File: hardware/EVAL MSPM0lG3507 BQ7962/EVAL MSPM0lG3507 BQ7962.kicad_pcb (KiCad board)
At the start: 2 copper layers, 72.5 x 101.3 mm, 155 parts, among them J1 Conn_01x09_Socket, J10 Screw_Terminal_01x02, J11 Screw_Terminal_01x02, J12 Screw_Terminal_01x02, J13 Screw_Terminal_01x02, J14 Screw_Terminal_01x02, J16 Conn_02x02_Odd_Even, J17 Conn_01x02_Pin, J18 Conn_01x02_Pin, J2 Conn_02x05_Odd_Even, J3 Conn_01x04_Pin, J4 Screw_Terminal_01x02, J5 Conn_01x03_Pin, J7 Screw_Terminal_01x02, J8 Screw_Terminal_01x02, J9 Screw_Terminal_01x02, SW1 SW_Push, SW2 SW_Push, SW3 SW_Push, U1 TPD6E004RSER, U10 MCP2542FDxMF, U11 FCX495, U2 MCU-MSM0G3507SPM, U3 TPD6E004RSER, U4 FCX495, U7 PBQ76952PFBT, U8 FCX495, U9 LMR51603XDBVR

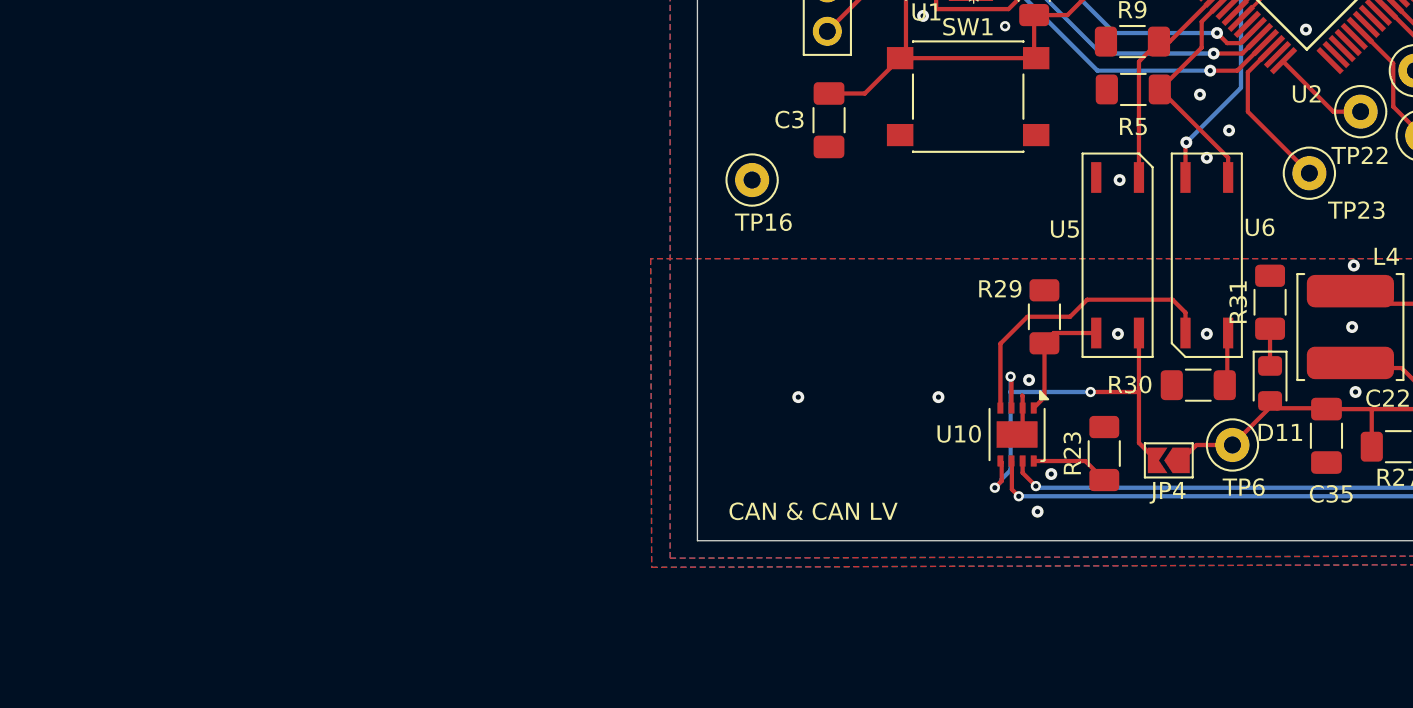
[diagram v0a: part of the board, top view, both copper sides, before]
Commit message: 07/15/25 - PCB Update
- Added the new footprint to the PCB file

Co-Authored-By: Görge Albrecht <617230+goerge@users.noreply.github.com>
Co-Authored-By: MarcusTurley <86125719+MarcusTurley@users.noreply.github.com>
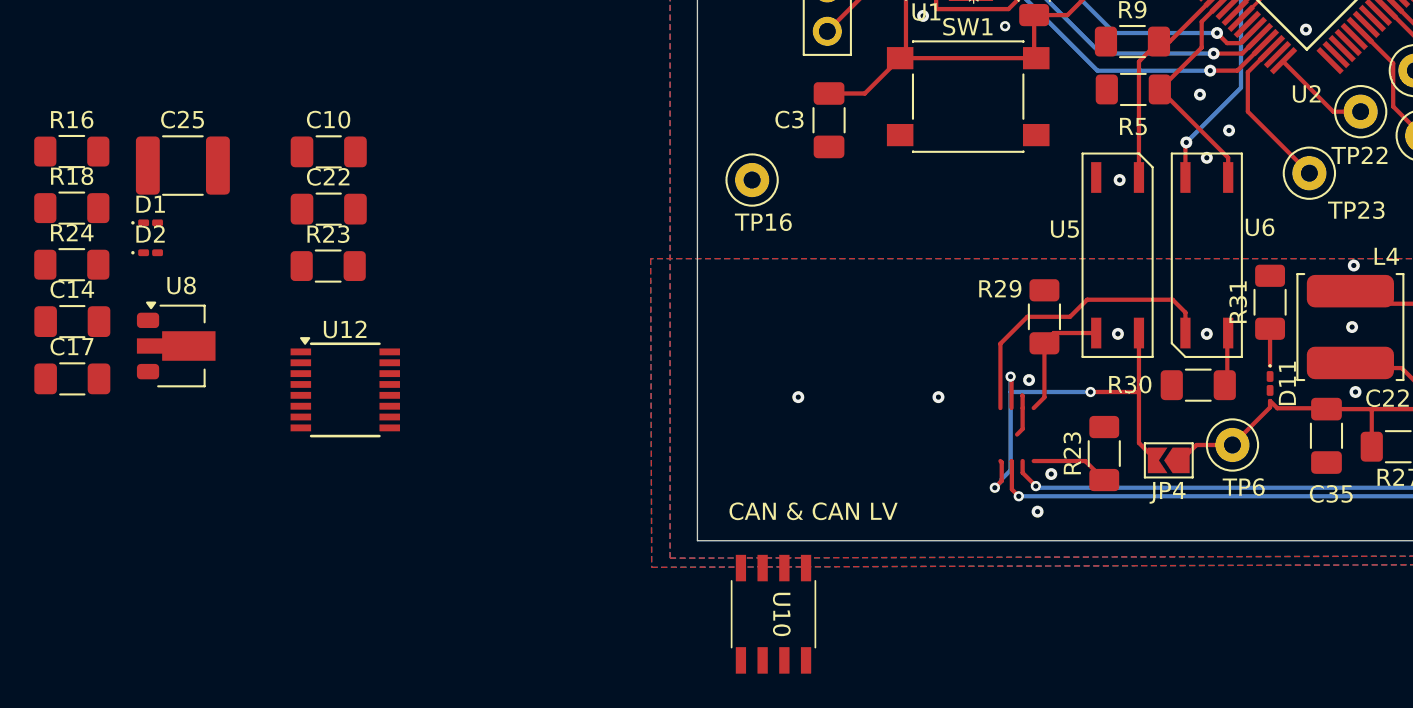
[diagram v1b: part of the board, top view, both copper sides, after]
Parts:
- added C10: 10u, Capacitor_SMD:C_1206_3216Metric_Pad1.33x1.80mm_HandSolder, F.Cu at (80.6, 102.4)
- added C14: 10u, Capacitor_SMD:C_1206_3216Metric_Pad1.33x1.80mm_HandSolder, F.Cu at (65.6, 112.3)
- added C17: 10u, Capacitor_SMD:C_1206_3216Metric_Pad1.33x1.80mm_HandSolder, F.Cu at (65.6, 115.6)
- added C22: 220n, Capacitor_SMD:C_1206_3216Metric_Pad1.33x1.80mm_HandSolder, F.Cu at (80.6, 105.7)
- added C25: 1u, Capacitor_SMD:C_1812_4532Metric, F.Cu at (72.1, 103.2)
- added D1: LED, LED_SMD:LED_0201_0603Metric_Pad0.64x0.40mm_HandSolder, F.Cu at (70.2, 106.5)
- added D2: LED, LED_SMD:LED_0201_0603Metric_Pad0.64x0.40mm_HandSolder, F.Cu at (70.2, 108.3)
- added R16: 5k, Resistor_SMD:R_1206_3216Metric_Pad1.30x1.75mm_HandSolder, F.Cu at (65.6, 102.3)
- added R18: 5k, Resistor_SMD:R_1206_3216Metric_Pad1.30x1.75mm_HandSolder, F.Cu at (65.6, 105.6)
- added R23: 50k, Resistor_SMD:R_1206_3216Metric_Pad1.30x1.75mm_HandSolder, F.Cu at (80.6, 109.0)
- added R24: 50k, Resistor_SMD:R_1206_3216Metric_Pad1.30x1.75mm_HandSolder, F.Cu at (65.6, 109.0)
- added U12: FT230XS, Package_SO:SSOP-16_3.9x4.9mm_P0.635mm, F.Cu at (81.6, 116.3)
- added U8: FCX495, Package_TO_SOT_SMD:SOT-89-3, F.Cu at (72.0, 113.7)
- C35: value 220n -> 10u
- D11: footprint LED_SMD:LED_0805_2012Metric_Pad1.15x1.40mm_HandSolder -> LED_SMD:LED_0201_0603Metric_Pad0.64x0.40mm_HandSolder
- R7: value 47k -> 50k
- U10: footprint Package_DFN_QFN:DFN-8-1EP_3x3mm_P0.65mm_EP1.55x2.4mm -> zzLocalLibraries-Footprints:SOIC-8_4.9x6.0mm_P1.27mm
- moved U10 17.7 mm to (106.6, 129.4)
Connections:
- C26 pad 1: Net-(D5-K) -> Net-(U7-BAT)
- C28 pad 1: Net-(D5-K) -> Net-(C28-Pad1)
- C39 pad 1: Net-(D5-K) -> Net-(U7-BAT)
- C40 pad 1: Net-(D5-K) -> Net-(U7-BAT)
- C41 pad 1: Net-(D5-K) -> Net-(U7-BAT)
- J1 pad 9: PA18 -> unconnected-(J1-Pin_9-Pad9)
- R1 pad 1: Net-(D4-K) -> Net-(D2-K)
- R11 pad 1: Net-(D5-K) -> Net-(U7-BAT)
- R11 pad 2: Net-(R11-Pad2) -> Net-(C25-Pad1)
- R47 pad 2: Net-(D5-K) -> Net-(U7-BAT)
- R49 pad 1: Net-(D5-K) -> Net-(U7-BAT)
- R6 pad 2: Net-(D3-K) -> Net-(D1-K)
- U1 pad 7: PA18 -> /XDS_BLS_INVOKE
- U4 pad 2: Net-(C42-Pad1) -> Net-(C25-Pad1)
- U7 pad 47: Net-(D5-K) -> Net-(U7-BAT)
- U9 pad 4: /GLV CAN TRX/+GLV regulated -> /GLV CAN TRX/+GLV
- U9 pad 5: /GLV CAN TRX/+GLV regulated -> /GLV CAN TRX/+GLV

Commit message: corrected MCP2542FS SOIC footprint pin numbering
marcus almost had it perfect. pads were in wrong order.

Co-Authored-By: George Boone <yongboone1@gmail.com>
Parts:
- turned U10 to 0 degrees
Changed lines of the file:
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@@
 	(footprint "zzLocalLibraries-Footprints:SOIC-8_4.9x6.0mm_P1.27mm"
 		(layer "F.Cu")
-		(at 106.6 129.4 -90)
+		(at 106.6 129.4)
 		(property "Reference" "U10"
-			(at 0 -0.5 270)
+			(at 0 -0.499999 0)
 			(unlocked yes)
 			(layer "F.SilkS")
@@
 		)
 		(property "Value" "MCP2542FDxMF"
-			(at 0 1 270)
+			(at 0 1 0)
 			(unlocked yes)
 			(layer "F.Fab")
@@
 		)
 		(property "Datasheet" "http://ww1.microchip.com/downloads/en/DeviceDoc/MCP2542FD-4FD-MCP2542WFD-4WFD-Data-Sheet20005514B.pdf"
-			(at 0 0 270)
+			(at 0 0 0)
 			(unlocked yes)
 			(layer "F.Fab")
@@
 		)
 		(property "Description" "CAN-FD Transceiver, Wake-Up on CAN activity, 8Mbps, 5V supply, STBY pin, 3x3 DFN-8"
-			(at 0 0 270)
+			(at 0 0 0)
 			(unlocked yes)
 			(layer "F.Fab")
@@
 		)
 		(property "Sim.Device" ""
-			(at 0 0 270)
+			(at 0 0 0)
 			(unlocked yes)
 			(layer "F.Fab")
@@
 		)
 		(property "Sim.Type" ""
-			(at 0 0 270)
+			(at 0 0 0)
 			(unlocked yes)
 			(layer "F.Fab")
@@
 		)
 		(fp_line
+			(start -3.55 -2.345)
+			(end -3.55 2.255)
+			(stroke
+				(width 0.05)
+				(type default)
+			)
+			(layer "F.CrtYd")
+		)
+		(fp_line
+			(start -3.55 2.255)
+			(end -1.95 2.255)
+			(stroke
+				(width 0.05)
+				(type default)
+			)
+			(layer "F.CrtYd")
+		)
+		(fp_line
+			(start -1.95 -2.545)
+			(end -1.95 -2.345)
+			(stroke
+				(width 0.05)
+				(type default)
+			)
+			(layer "F.CrtYd")
+		)
+		(fp_line
+			(start -1.95 -2.345)
+			(end -3.55 -2.345)
+			(stroke
+				(width 0.05)
+				(type default)
+			)
+			(layer "F.CrtYd")
+		)
+		(fp_line
+			(start -1.95 2.255)
+			(end -1.95 2.455)
+			(stroke
+				(width 0.05)
+				(type default)
+			)
+			(layer "F.CrtYd")
+		)
+		(fp_line
 			(start -1.95 2.455)
 			(end 1.95 2.455)
@@
 		)
 		(fp_line
+			(start 1.95 -2.545)
+			(end -1.95 -2.545)
+			(stroke
+				(width 0.05)
+				(type default)
+			)
+			(layer "F.CrtYd")
+		)
+		(fp_line
+			(start 1.95 -2.345)
+			(end 1.95 -2.545)
+			(stroke
+				(width 0.05)
+				(type default)
+			)
+			(layer "F.CrtYd")
+		)
+		(fp_line
 			(start 1.95 2.455)
 			(end 1.95 2.255)
@@
 		)
 		(fp_line
-			(start -3.55 2.255)
-			(end -1.95 2.255)
-			(stroke
-				(width 0.05)
-				(type default)
-			)
-			(layer "F.CrtYd")
-		)
-		(fp_line
-			(start -1.95 2.255)
-			(end -1.95 2.455)
-			(stroke
-				(width 0.05)
-				(type default)
-			)
-			(layer "F.CrtYd")
-		)
-		(fp_line
-			(start 1.95 2.255)
-			(end 3.55 2.255)
-			(stroke
-				(width 0.05)
-				(type default)
-			)
-			(layer "F.CrtYd")
-		)
-		(fp_line
-			(start 3.55 2.255)
-			(end 3.55 -2.345)
-			(stroke
-				(width 0.05)
-				(type default)
-			)
-			(layer "F.CrtYd")
-		)
-		(fp_line
-			(start -3.55 -2.345)
-			(end -3.55 2.255)
-			(stroke
-				(width 0.05)
-				(type default)
-			)
-			(layer "F.CrtYd")
-		)
-		(fp_line
-			(start -1.95 -2.345)
-			(end -3.55 -2.345)
-			(stroke
-				(width 0.05)
-				(type default)
-			)
-			(layer "F.CrtYd")
-		)
-		(fp_line
-			(start 1.95 -2.345)
-			(end 1.95 -2.545)
-			(stroke
-				(width 0.05)
-				(type default)
-			)
-			(layer "F.CrtYd")
-		)
-		(fp_line
 			(start 3.55 -2.345)
 			(end 1.95 -2.345)
@@
 		)
 		(fp_line
-			(start -1.95 -2.545)
-			(end -1.95 -2.345)
-			(stroke
-				(width 0.05)
-				(type default)
-			)
-			(layer "F.CrtYd")
-		)
-		(fp_line
-			(start 1.95 -2.545)
-			(end -1.95 -2.545)
+			(start 3.55 2.25)
+			(end 1.95 2.25)
+			(stroke
+				(width 0.05)
+				(type default)
+			)
+			(layer "F.CrtYd")
+		)
+		(fp_line
+			(start 3.55 2.25)
+			(end 3.55 -2.345)
 			(stroke
 				(width 0.05)
@@
 		)
 		(fp_text user "${REFERENCE}"
-			(at 0 2.5 270)
+			(at 0 2.5 0)
 			(unlocked yes)
 			(layer "F.Fab")
@@
 		)
 		(pad "1" smd rect
-			(at -2.7 -1.955 270)
+			(at -2.7 -1.955)
 			(size 1.55 0.6)
 			(layers "F.Cu" "F.Mask" "F.Paste")
@@
 		)
 		(pad "2" smd rect
-			(at -2.7 -0.685 270)
+			(at -2.7 -0.685)
 			(size 1.55 0.6)
 			(layers "F.Cu" "F.Mask" "F.Paste")
@@
 		)
 		(pad "3" smd rect
-			(at -2.7 0.585 270)
+			(at -2.7 0.585)
 			(size 1.55 0.6)
 			(layers "F.Cu" "F.Mask" "F.Paste")
@@
 		)
 		(pad "4" smd rect
-			(at -2.7 1.855 270)
+			(at -2.7 1.855)
 			(size 1.55 0.6)
 			(layers "F.Cu" "F.Mask" "F.Paste")
@@
 		)
 		(pad "5" smd rect
-			(at 2.7 -1.955 270)
+			(at 2.7 1.86 180)
 			(size 1.55 0.6)
 			(layers "F.Cu" "F.Mask" "F.Paste")
@@
 		)
 		(pad "6" smd rect
-			(at 2.7 0.585 270)
+			(at 2.7 0.58)
 			(size 1.55 0.6)
 			(layers "F.Cu" "F.Mask" "F.Paste")
@@
 		)
 		(pad "7" smd rect
-			(at 2.7 -0.685 270)
+			(at 2.7 -0.69)
 			(size 1.55 0.6)
 			(layers "F.Cu" "F.Mask" "F.Paste")
@@
 		)
 		(pad "8" smd rect
-			(at 2.7 1.855 270)
-			(size 1.55 0.6)
-			(layers "F.Cu" "F.Mask" "F.Paste")
+			(at 2.7 -1.95 180)
+			(size 1.55 0.6)
+			(layers "F.Cu" "F.Mask" "F.Paste")

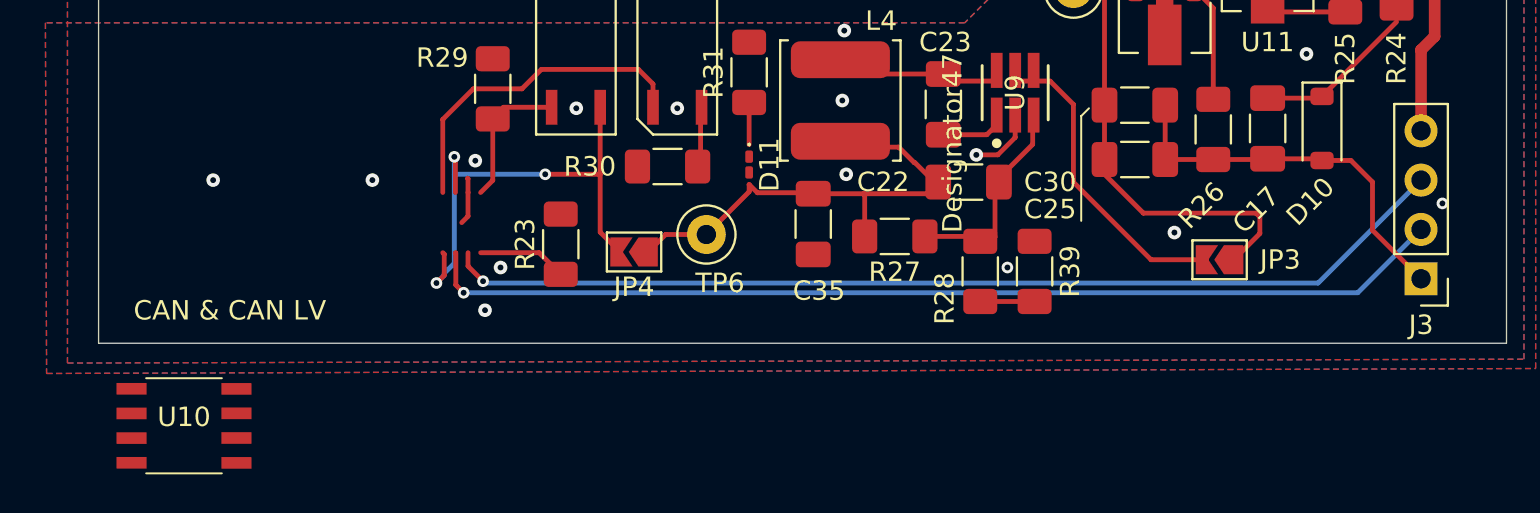
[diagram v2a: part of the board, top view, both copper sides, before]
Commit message: made a hierarchical sheet for the BQ chip
Co-Authored-By: George Boone <yongboone1@gmail.com>
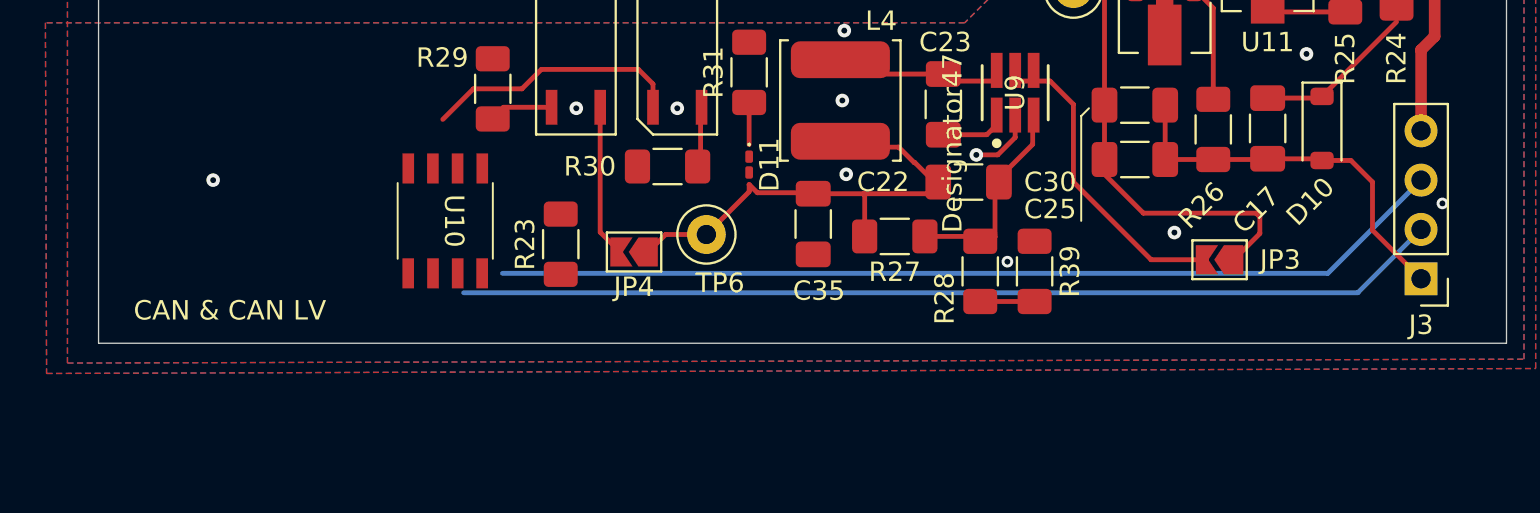
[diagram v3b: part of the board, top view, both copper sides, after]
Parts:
- moved U10 17.1 mm to (120.0, 118.8), turned to -90 degrees
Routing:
- net /GLV CAN TRX/5v: track 25.9 -> 7.87 mm, vias 3 -> 0
- net Net-(U10-STBY): track 4.59 -> 0.00 mm
- net Net-(U10-TXD): track 7.45 -> 3.41 mm
- net Net-(U10-RXD): track 17.2 -> 13.4 mm
- net /GLV CAN TRX/CAN_H: track 52.4 -> 49.3 mm, vias 1 -> 0
- net /GLV CAN TRX/-GLV: track 26.4 -> 24.0 mm, vias 16 -> 12
- net /GLV CAN TRX/CAN_L: track 52.9 -> 50.7 mm, vias 1 -> 0

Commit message: mouser doom scrolling labor
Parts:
- removed C12, C13, C16, C17, C18, C19, C20, C21, C24, C25, C27, C29, C31, C32, C33, C7, C8, C9: 220n, Capacitor_SMD:C_1206_3216Metric_Pad1.33x1.80mm_HandSolder
- removed the C14 at (155.9, 88.7)
- removed C17: 10u, Capacitor_SMD:C_1206_3216Metric_Pad1.33x1.80mm_HandSolder
- removed the C22 at (147.0, 116.8)
- removed C25: 1u, Capacitor_SMD:C_1812_4532Metric
- removed C26, C28, C39, C40, C41: 100n, Capacitor_SMD:C_1206_3216Metric_Pad1.33x1.80mm_HandSolder
- removed D10: 36V, Diode_SMD:D_SOD-123
- removed D4: LED, LED_SMD:LED_0805_2012Metric_Pad1.15x1.40mm_HandSolder
- removed D5: 100V, Diode_SMD:D_1206_3216Metric_Pad1.42x1.75mm_HandSolder
- removed J16: Conn_02x02_Odd_Even, Connector_PinHeader_2.54mm:PinHeader_2x02_P2.54mm_Vertical
- removed J18: Conn_01x02_Pin, Connector_PinHeader_2.54mm:PinHeader_1x02_P2.54mm_Vertical
- removed JP3: SolderJumper_2_Open, Jumper:SolderJumper-2_P1.3mm_Open_TrianglePad1.0x1.5mm
- removed the R16 at (131.8, 67.2)
- removed the R18 at (157.2, 64.0)
- removed the R23 at (126.0, 120.0)
- removed the R24 at (65.6, 109.0)
- removed the R24 at (169.0, 106.3)
- removed R47, R48, R49: 5k, Resistor_SMD:R_1206_3216Metric_Pad1.30x1.75mm_HandSolder
- removed SW2, SW3: SW_Push, Button_Switch_SMD:SW_SPST_PTS645
- removed TP19, TP20, TP8: TestPoint, TestPoint:TestPoint_Loop_D2.50mm_Drill1.0mm_LowProfile
- removed U1, U3: TPD6E004RSER, zzLocalLibraries-Footprints:RSE8
- removed U4, U8 (x2): FCX495, Package_TO_SOT_SMD:SOT-89-3
- removed U7: PBQ76952PFBT, zzLocalLibraries-Footprints:BQ76952_PFB48_TEX
- added C37: 220n, Capacitor_SMD:C_1206_3216Metric_Pad1.33x1.80mm_HandSolder, F.Cu at (41.5, 163.8)
- added C38: 220n, Capacitor_SMD:C_1206_3216Metric_Pad1.33x1.80mm_HandSolder, F.Cu at (47.6, 140.4)
- added C43: 220n, Capacitor_SMD:C_1206_3216Metric_Pad1.33x1.80mm_HandSolder, F.Cu at (47.6, 147.1)
- added C44: 220n, Capacitor_SMD:C_1206_3216Metric_Pad1.33x1.80mm_HandSolder, F.Cu at (47.6, 150.4)
- added C45: 220n, Capacitor_SMD:C_1206_3216Metric_Pad1.33x1.80mm_HandSolder, F.Cu at (47.6, 153.8)
- added C46: 220n, Capacitor_SMD:C_1206_3216Metric_Pad1.33x1.80mm_HandSolder, F.Cu at (47.6, 157.1)
- added C47: 220n, Capacitor_SMD:C_1206_3216Metric_Pad1.33x1.80mm_HandSolder, F.Cu at (47.6, 160.5)
- added C48: 220n, Capacitor_SMD:C_1206_3216Metric_Pad1.33x1.80mm_HandSolder, F.Cu at (47.6, 163.8)
- added C49: 220n, Capacitor_SMD:C_1206_3216Metric_Pad1.33x1.80mm_HandSolder, F.Cu at (53.6, 140.4)
- added C50: 220n, Capacitor_SMD:C_1206_3216Metric_Pad1.33x1.80mm_HandSolder, F.Cu at (53.6, 143.7)
- added C51: 220n, Capacitor_SMD:C_1206_3216Metric_Pad1.33x1.80mm_HandSolder, F.Cu at (53.6, 147.1)
- added C52: 220n, Capacitor_SMD:C_1206_3216Metric_Pad1.33x1.80mm_HandSolder, F.Cu at (53.6, 150.4)
- added C53: 220n, Capacitor_SMD:C_1206_3216Metric_Pad1.33x1.80mm_HandSolder, F.Cu at (53.6, 153.8)
- added C54: 220n, Capacitor_SMD:C_1206_3216Metric_Pad1.33x1.80mm_HandSolder, F.Cu at (53.6, 157.1)
- added C55: 220n, Capacitor_SMD:C_1206_3216Metric_Pad1.33x1.80mm_HandSolder, F.Cu at (53.6, 160.5)
- added C56: 100n, Capacitor_SMD:C_1206_3216Metric_Pad1.33x1.80mm_HandSolder, F.Cu at (53.6, 163.8)
- added C57: 10u, Capacitor_SMD:C_1206_3216Metric_Pad1.33x1.80mm_HandSolder, F.Cu at (59.6, 140.4)
- added C58: 100n, Capacitor_SMD:C_1206_3216Metric_Pad1.33x1.80mm_HandSolder, F.Cu at (59.6, 143.7)
- added C59: 100n, Capacitor_SMD:C_1206_3216Metric_Pad1.33x1.80mm_HandSolder, F.Cu at (59.6, 147.1)
- added C60: 100n, Capacitor_SMD:C_1206_3216Metric_Pad1.33x1.80mm_HandSolder, F.Cu at (59.6, 150.4)
- added C61: 100n, Capacitor_SMD:C_1206_3216Metric_Pad1.33x1.80mm_HandSolder, F.Cu at (59.6, 153.8)
- added C62: 1u, Capacitor_SMD:C_1812_4532Metric, F.Cu at (42.1, 179.9)
- added J15: Conn_01x02_Pin, Connector_PinHeader_2.54mm:PinHeader_1x02_P2.54mm_Vertical, F.Cu at (94.0, 164.2)
- added J6: Conn_01x02_Pin, Connector_PinHeader_2.54mm:PinHeader_1x02_P2.54mm_Vertical, F.Cu at (89.4, 164.2)
- added Q1: ~, zzLocalLibraries-Footprints:SOT8001, F.Cu at (97.1, 168.1)
- added R24: 50, Resistor_SMD:R_1206_3216Metric_Pad1.30x1.75mm_HandSolder, F.Cu at (65.6, 153.6)
- added R65: 50k, Resistor_SMD:R_1206_3216Metric_Pad1.30x1.75mm_HandSolder, F.Cu at (77.5, 153.6)
- added R72: 200, Resistor_SMD:R_1206_3216Metric_Pad1.30x1.75mm_HandSolder, F.Cu at (77.5, 156.9)
- added TH3: Thermistor_US, Resistor_SMD:R_1206_3216Metric_Pad1.30x1.75mm_HandSolder, F.Cu at (96.0, 153.6)
- added TH4: Thermistor_US, Resistor_SMD:R_1206_3216Metric_Pad1.30x1.75mm_HandSolder, F.Cu at (96.0, 156.9)
- added TH5: Thermistor_US, Resistor_SMD:R_1206_3216Metric_Pad1.30x1.75mm_HandSolder, F.Cu at (96.0, 160.2)
- added TH6: Thermistor_US, Resistor_SMD:R_1206_3216Metric_Pad1.30x1.75mm_HandSolder, F.Cu at (102.0, 140.4)
- added TH7: Thermistor_US, Resistor_SMD:R_1206_3216Metric_Pad1.30x1.75mm_HandSolder, F.Cu at (102.0, 143.7)
- added TH8: Thermistor_US, Resistor_SMD:R_1206_3216Metric_Pad1.30x1.75mm_HandSolder, F.Cu at (102.0, 147.0)
- added TH9: Thermistor_US, Resistor_SMD:R_1206_3216Metric_Pad1.30x1.75mm_HandSolder, F.Cu at (102.0, 150.3)
- added TP1: TestPoint, TestPoint:TestPoint_Loop_D2.50mm_Drill1.0mm_LowProfile, F.Cu at (58.9, 167.8)
- added TP13: TestPoint, TestPoint:TestPoint_Loop_D2.50mm_Drill1.0mm_LowProfile, F.Cu at (84.8, 155.0)
- added TP18: TestPoint, TestPoint:TestPoint_Loop_D2.50mm_Drill1.0mm_LowProfile, F.Cu at (58.9, 181.8)
- added U13: PBQ76952PFBT, zzLocalLibraries-Footprints:BQ76952_PFB48_TEX, F.Cu at (44.5, 171.5)
- added U14: FCX495, Package_TO_SOT_SMD:SOT-89-3, F.Cu at (53.8, 174.7)
- C1, C4: value 100n -> 10u
- C2: value 220n -> 10u
- C30: value 220n -> 100n
- C34: value 2.2u -> 100p; footprint Capacitor_THT:CP_Radial_D8.0mm_P2.50mm -> Capacitor_SMD:C_1206_3216Metric_Pad1.33x1.80mm_HandSolder
- C36, C42: value 2.2u -> 220n; footprint Capacitor_THT:CP_Radial_D8.0mm_P2.50mm -> Capacitor_SMD:C_1206_3216Metric_Pad1.33x1.80mm_HandSolder
- C6: value 100p -> 10u
- D3: value LED -> D_Zener_Small; footprint LED_SMD:LED_0805_2012Metric_Pad1.15x1.40mm_HandSolder -> Diode_SMD:D_SOD-123
- R10, R13, R14: value 50 -> 5k
- R11: value 200 -> 50k
- R17: value 50 -> 150
- R2: value 5k -> 50k
- R25: value 47k -> 100
- R26: value 10M -> 100
- R37, R38: value 100 -> 50
- R4: value 100 -> 150
- R40: value 5k -> 50
- R45: value 5k -> 200
- R46: value 100 -> 5k
- TP9: footprint TestPoint:TestPoint_Loop_D2.50mm_Drill1.0mm_LowProfile -> TestPoint:TestPoint_THTPad_3.0x3.0mm_Drill1.5mm
- moved C36 172.1 mm to (41.5, 160.5), turned to 0 degrees
- moved R41 147.7 mm to (71.5, 163.5), turned to 0 degrees
- moved C42 144.6 mm to (47.6, 143.7)
- moved D3 143.8 mm to (53.4, 179.4), turned to 0 degrees
- moved C1 140.2 mm to (41.5, 140.4), turned to 0 degrees
- moved R32 137.9 mm to (65.6, 163.5), turned to 0 degrees
- moved TP9 133.4 mm to (98.8, 164.4)
- moved R44 132.4 mm to (77.5, 147.0), turned to 0 degrees
- moved R43 131.5 mm to (77.5, 143.7), turned to 0 degrees
- moved R36 129.0 mm to (71.5, 150.3), turned to 0 degrees
- moved R22 127.8 mm to (65.6, 150.3), turned to 0 degrees
- moved R35 127.8 mm to (71.5, 147.0), turned to 0 degrees
- moved TP2 127.7 mm to (58.9, 172.5)
- moved R34 126.7 mm to (71.5, 143.7), turned to 0 degrees
- moved R21 126.5 mm to (65.6, 147.0), turned to 0 degrees
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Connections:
- C1 pad 1: onboard 3.3v src -> Net-(U13-BAT)
- C2 pad 1: Net-(U7-VC0) -> Net-(U13-BAT)
- C30 pad 1: Net-(JP3-A) -> Net-(U13-SRP)
- C30 pad 2: /GLV CAN TRX/-GLV -> Net-(U13-SRN)
- C34 pad 1: Net-(U7-REG18) -> Net-(U13-SRP)
- C34 pad 2: GND -> Net-(U13-SRN)
- C36 pad 1: Net-(D5-K) -> Net-(U13-VC16)
- C36 pad 2: GND -> Net-(U13-VC15)
- C4 pad 1: Net-(U7-SRP) -> Net-(U13-BAT)
- C4 pad 2: Net-(U7-SRN) -> GND
- C42 pad 1: Net-(C42-Pad1) -> Net-(U13-VC10)
- C42 pad 2: GND -> Net-(U13-VC9)
- C6 pad 1: Net-(U7-SRP) -> Net-(U13-BAT)
- C6 pad 2: Net-(U7-SRN) -> GND
- D3 pad 1: Net-(D3-K) -> unconnected-(D3-K-Pad1)
- D3 pad 2: VDD -> unconnected-(D3-A-Pad2)
- J10 pad 1: /8P -> /BQ76952 16C/8P
- J10 pad 2: /9P -> /BQ76952 16C/9P
- J11 pad 1: /10P -> /BQ76952 16C/10P
- J11 pad 2: /11P -> /BQ76952 16C/11P
- J12 pad 1: /12P -> /BQ76952 16C/12P
- J12 pad 2: /13P -> /BQ76952 16C/13P
- J13 pad 1: /14P -> /BQ76952 16C/14P
- J13 pad 2: /15P -> /BQ76952 16C/15P
- J4 pad 2: /1P -> /BQ76952 16C/1P
- J7 pad 1: /2P -> /BQ76952 16C/2P
- J7 pad 2: /3P -> /BQ76952 16C/3P
- J8 pad 1: /4P -> /BQ76952 16C/4P
- J8 pad 2: /5P -> /BQ76952 16C/5P
- J9 pad 1: /6P -> /BQ76952 16C/6P
- J9 pad 2: /7P -> /BQ76952 16C/7P
- R10 pad 1: -BATT -> Net-(R10-Pad1)
- R10 pad 2: Net-(U7-VC0) -> /BAT
- R11 pad 1: Net-(U7-BAT) -> GND
- R11 pad 2: Net-(C25-Pad1) -> /BQ76952 16C/RST_SHUT
- R13 pad 1: /1P -> /BQ76952 16C/PACK
- R13 pad 2: Net-(U7-VC1) -> Net-(R10-Pad1)
- R14 pad 1: /2P -> /BAT
- R14 pad 2: Net-(U7-VC2) -> /BQ76952 16C/LD
- R15 pad 1: Net-(U7-ALERT) -> Net-(J6-Pin_2)
- R15 pad 2: GND -> /BQ0_3.3v
- R17 pad 1: /3P -> Net-(J6-Pin_1)
- R17 pad 2: Net-(U7-VC3) -> /BQ76952 16C/SDA
- R19 pad 1: /4P -> /BQ76952 16C/15P
- R19 pad 2: Net-(U7-VC4) -> Net-(U13-VC15)
- R2 pad 2: Net-(U7-RST_SHUT) -> PB26
- R20 pad 1: /8P -> /BQ76952 16C/14P
- R21 pad 1: /7P -> /BQ76952 16C/13P
- R22 pad 1: /6P -> /BQ76952 16C/12P
- R25 pad 1: Net-(R25-Pad1) -> -BATT
- R25 pad 2: /GLV CAN TRX/+GLV -> Net-(U13-SRP)
- R26 pad 1: /GLV CAN TRX/-GLV -> GND
- R26 pad 2: Net-(R26-Pad2) -> Net-(U13-SRN)
- R32 pad 1: /5P -> /BQ76952 16C/10P
- R32 pad 2: Net-(U7-VC5) -> Net-(U13-VC10)
- R33 pad 1: /12P -> /BQ76952 16C/9P
- R33 pad 2: Net-(U7-VC12) -> Net-(U13-VC9)
- R34 pad 1: /11P -> /BQ76952 16C/8P
- R35 pad 1: /10P -> /BQ76952 16C/7P
- R36 pad 1: /9P -> /BQ76952 16C/6P
- R37 pad 1: -BATT -> /BQ76952 16C/5P
- R37 pad 2: Net-(U7-SRP) -> Net-(U13-VC5)
- R38 pad 1: GND -> /BQ76952 16C/4P
- R38 pad 2: Net-(U7-SRN) -> Net-(U13-VC4)
- R4 pad 1: Net-(U7-SDA) -> /BQ76952 16C/SCL
- R4 pad 2: Net-(J16-Pin_1) -> Net-(J6-Pin_2)
- R40 pad 1: Net-(R40-Pad1) -> +BATT
- R40 pad 2: Net-(J18-Pin_2) -> Net-(U13-VC16)
- R41 pad 1: /14P -> /BQ76952 16C/3P
- R42 pad 1: /13P -> /BQ76952 16C/2P
- R43 pad 1: +BATT -> /BQ76952 16C/1P
- R44 pad 1: /15P -> -BATT
- R45 pad 1: GND -> Net-(R45-Pad1)
- R45 pad 2: Net-(R40-Pad1) -> +BATT
- R46 pad 1: Net-(J16-Pin_3) -> Net-(J6-Pin_1)
- R46 pad 2: Net-(U7-SCL) -> /BQ0_3.3v
- TH1 pad 1: GND -> /BQ76952 16C/TS1
- TH1 pad 2: Net-(U7-TS1) -> GND
- TH2 pad 1: GND -> /BQ76952 16C/TS2
- TH2 pad 2: Net-(U7-TS3) -> GND
- TP10 pad 1: Net-(U7-TS3) -> Net-(J6-Pin_2)
- TP11 pad 1: Net-(U7-REG18) -> Net-(J6-Pin_1)
- TP17 pad 1: +5V -> PA16_I2C1_SDA
- TP2 pad 1: Net-(U7-SRP) -> Net-(U13-REGIN)
- TP3 pad 1: Net-(U7-SRN) -> Net-(U2-VCORE)
- TP7 pad 1: Net-(JP3-A) -> Net-(U13-SRN)
- TP9 pad 1: Net-(U7-TS1) -> GND
- U11 pad 2: Net-(R25-Pad1) -> Net-(R45-Pad1)
- U11 pad 3: Net-(R26-Pad2) -> Net-(U13-BAT)
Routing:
- net (no net): track 0.00 -> 792.7 mm, vias 0 -> 8
- net Net-(U7-TS1): track 44.0 -> 0.00 mm, vias 2 -> 0
- net Net-(U7-RST_SHUT): track 41.1 -> 0.00 mm, vias 2 -> 0
- net Net-(D5-K): track 41.1 -> 0.00 mm
- net Net-(J18-Pin_1): track 31.5 -> 0.00 mm
- net Net-(U7-VC0): track 29.9 -> 0.00 mm
- net Net-(U13-VC1): track 29.6 -> 0.00 mm
- net Net-(U13-VC0): track 27.8 -> 0.00 mm
- net Net-(U7-CP1): track 27.4 -> 0.00 mm, vias 2 -> 0
- net Net-(U7-VC1): track 25.6 -> 0.00 mm
- net Net-(U13-VC3): track 25.6 -> 0.00 mm
- net Net-(U7-SRN): track 25.0 -> 0.00 mm
- net Net-(JP3-A): track 24.4 -> 0.00 mm
- net Net-(C42-Pad1): track 24.2 -> 0.00 mm
- net Net-(U13-VC2): track 24.0 -> 0.00 mm
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- added copper zone on B.Cu, net /BQ76952 16C/2P
- removed copper zone on B.Cu, net /2P
